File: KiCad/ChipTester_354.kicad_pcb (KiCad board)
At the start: 2 copper layers, 172 x 61.5 mm, 55 parts, among them U1 TLE2426xP, U2 L7805, U3 TLE2426xP, U4 TLE2426xP, U5 MCP6002-xP

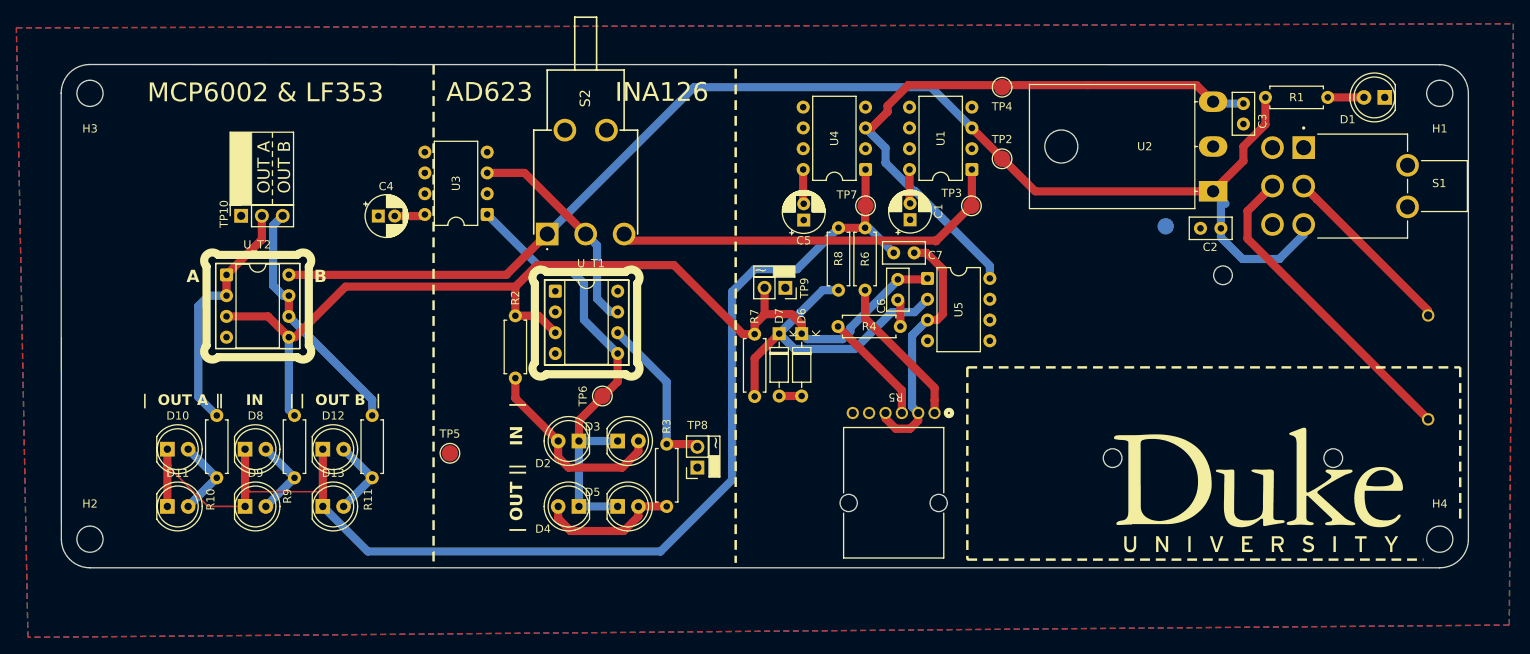
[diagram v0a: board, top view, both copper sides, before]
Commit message: Added milling machine files / updated schematic+pcb annotations /  updated footprints
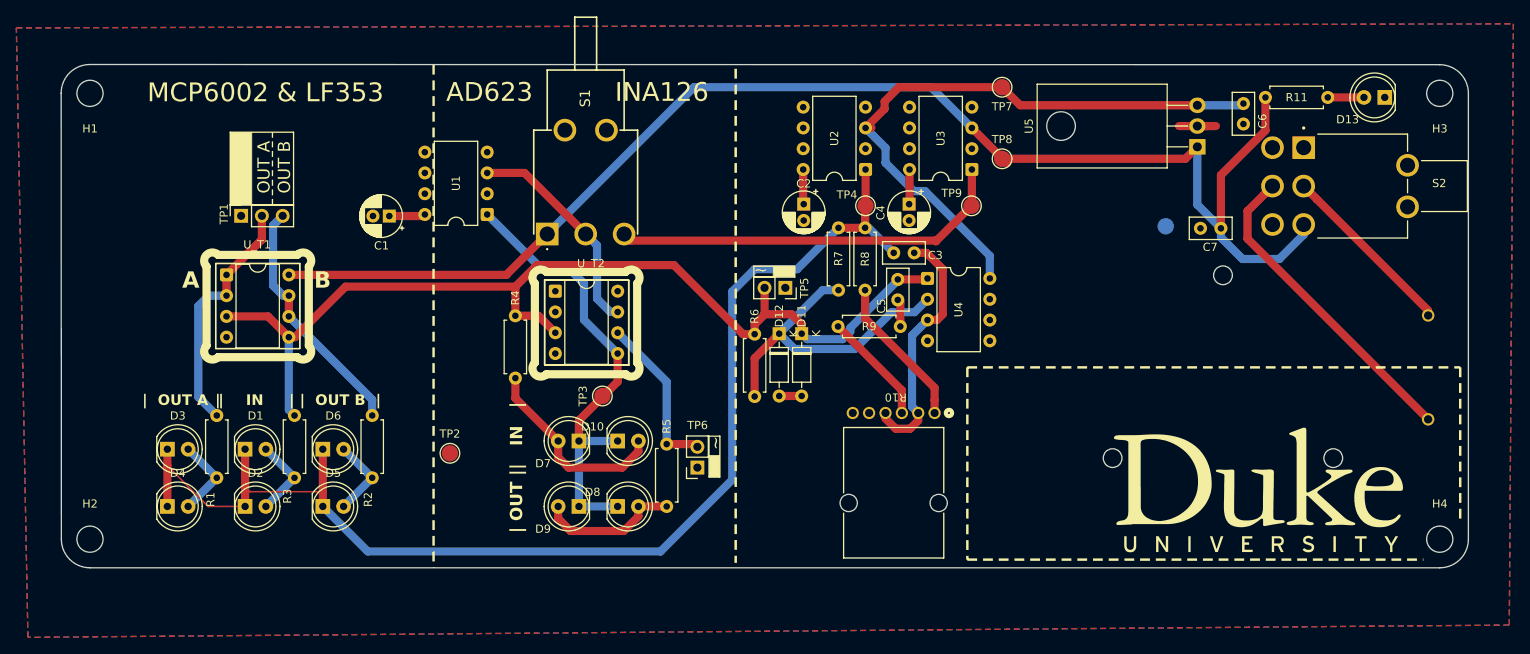
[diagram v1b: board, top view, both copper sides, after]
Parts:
- U5: renamed from U2; footprint Package_TO_SOT_THT:TO-218-3_Horizontal_TabDown -> Package_TO_SOT_THT:TO-220-3_Horizontal_TabDown
- moved U5 5.77 mm to (204.2, 63.5)
- moved C2 1.96 mm to (156.1, 70.5), turned to -90 degrees
- moved C4 1.91 mm to (169.0, 70.5), turned to -90 degrees
- moved C1 1.34 mm to (105.5, 72.0), turned to 180 degrees
- renumbered C4 to C1, C5 to C2, C7 to C3, C1 to C4, C6 to C5, C3 to C6, C2 to C7, D8 to D1, D3 to D10, D6 to D11, D7 to D12, D1 to D13, D9 to D2, D10 to D3, D11 to D4, D13 to D5, D12 to D6, D2 to D7, D5 to D8, D4 to D9, H3 to H1, H1 to H3, R10 to R1, R5 to R10, R1 to R11, R11 to R2, R9 to R3, R2 to R4, R3 to R5, R7 to R6, R8 to R7, R6 to R8, R4 to R9, S2 to S1, S1 to S2, TP10 to TP1, TP1 to TP10, TP5 to TP2, TP6 to TP3, TP7 to TP4, TP9 to TP5, TP8 to TP6, TP4 to TP7, TP2 to TP8, TP3 to TP9, U3 to U1, U4 to U2, U1 to U3, U5 to U4, U_T2 to U_T1, U_T1 to U_T2
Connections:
- C1 pad 1: GND -> Net-(U1-NOISE_REDUCTION)
- C1 pad 2: Net-(U3-NOISE_REDUCTION) -> GND
- C2 pad 1: GND -> Net-(U2-NOISE_REDUCTION)
- C2 pad 2: Net-(U4-NOISE_REDUCTION) -> GND
- C4 pad 1: GND -> Net-(U3-NOISE_REDUCTION)
- C4 pad 2: Net-(U1-NOISE_REDUCTION) -> GND
- U1 pad 8: Net-(U3-NOISE_REDUCTION) -> Net-(U1-NOISE_REDUCTION)
- U2 pad 8: Net-(U4-NOISE_REDUCTION) -> Net-(U2-NOISE_REDUCTION)
- U3 pad 8: Net-(U1-NOISE_REDUCTION) -> Net-(U3-NOISE_REDUCTION)
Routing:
- net +5V: track 86.5 -> 76.4 mm
- net +9V: track 164.6 -> 170.7 mm
- net GND: track 0.00 -> 5.77 mm
- net Net-(U4-NOISE_REDUCTION): track 4.22 -> 0.00 mm
- net Net-(U2-NOISE_REDUCTION): track 0.00 -> 4.22 mm
